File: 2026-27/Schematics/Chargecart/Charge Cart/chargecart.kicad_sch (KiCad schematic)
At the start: 27 parts, among them J1 UPCR012ALS1, J2 DTM04-12PA-L012, J3 NEMA_5-20, J4 TSMP, J5 J1772, K1 Charger Safety Relay, SW1 LV Switch, SW2 Charging Stop, SW3 LV Switch, SW4 Reset, U1 Milwaukee M12 Adapter, U3 Relay_Board, U4 6.6kW Elcon Charger

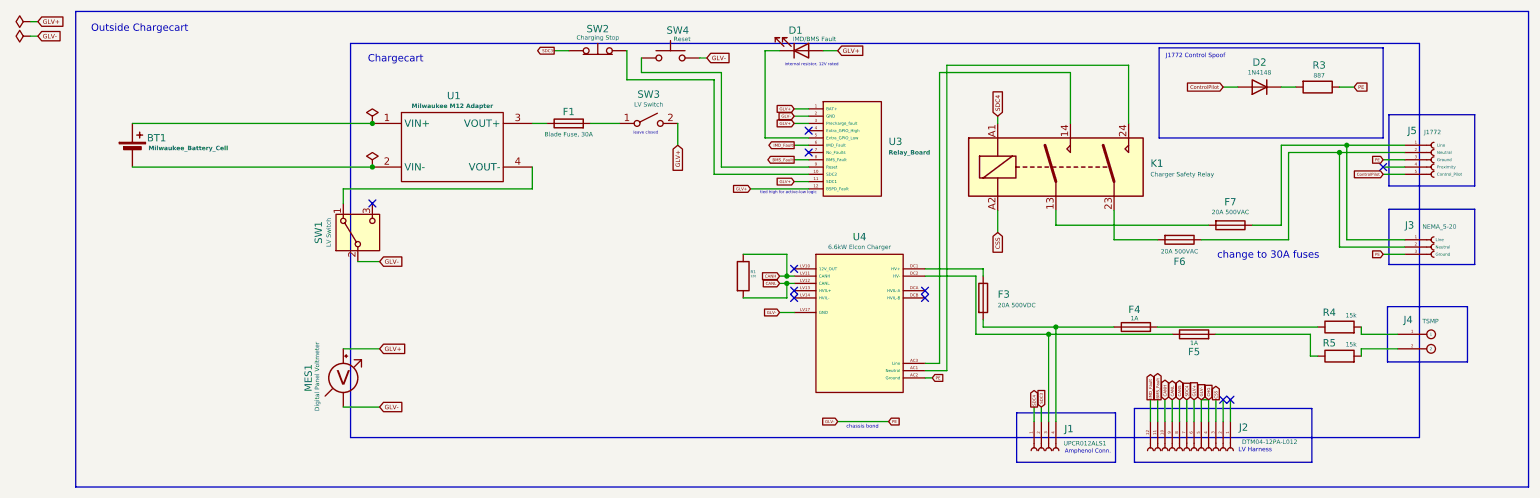
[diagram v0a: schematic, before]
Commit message: Update charge cart schematic with HVBP
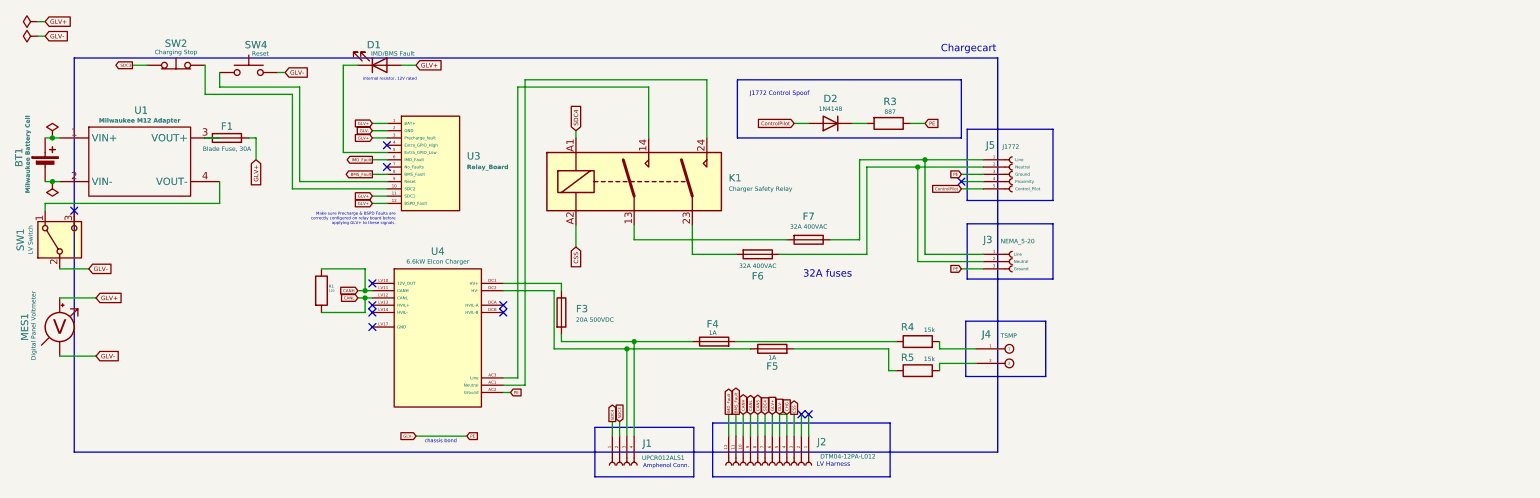
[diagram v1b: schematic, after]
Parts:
- removed SW3: LV Switch, symbol Switch:SW_SPST
- BT1: value Milwaukee_Battery_Cell -> Milwaukee Battery Cell
- F6, F7: value 20A 500VAC -> 32A 400VAC
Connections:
- net CHG: no longer U4.LV17 (GND)
- net GLV+: now also F1.2
- no-connect marks 11 -> 12
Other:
- note added: "32A fuses"
- note added: "Make sure Precharge & BSPD Faults are correctly configured on relay board before applying GLV+ to these signals."
- note removed: "Outside Chargecart"
- note removed: "change to 30A fuses"
- note removed: "leave closed"
- note removed: "tied high for active-low logic"
- moved on the sheet: BT1, D1, D2, F1, F3, F4, F5, F6, F7, J1, J2, J3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
